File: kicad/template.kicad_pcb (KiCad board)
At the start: 2 copper layers, 84.1 x 61.7 mm, 7 parts, among them J1 Bus_PCI_Express_x1, J6 USB_C_Receptacle_USB2.0_16P, U1 MCP25625T-E/ML, U2 RP2040, U4 W25Q128JVP, X1 ABM8-272-T3, Y1 X322516MLB4SI

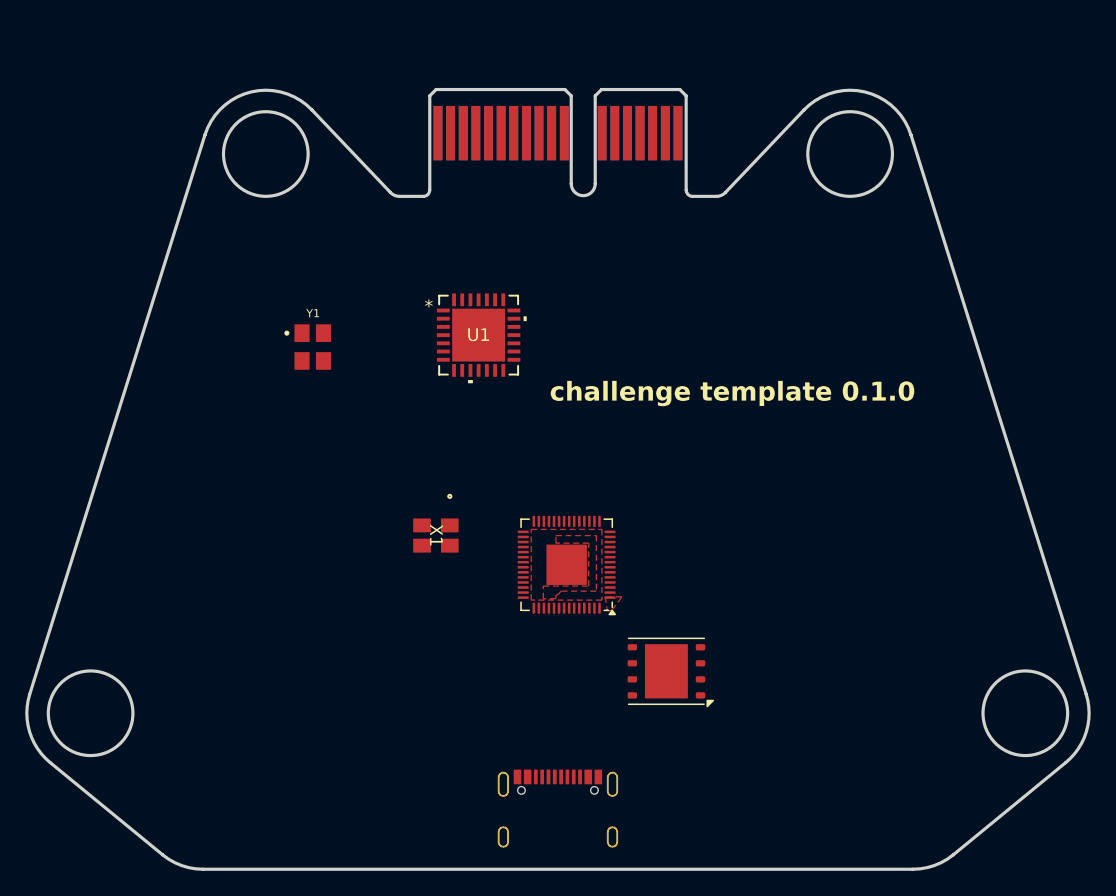
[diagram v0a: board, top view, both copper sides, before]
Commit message: Add LED array
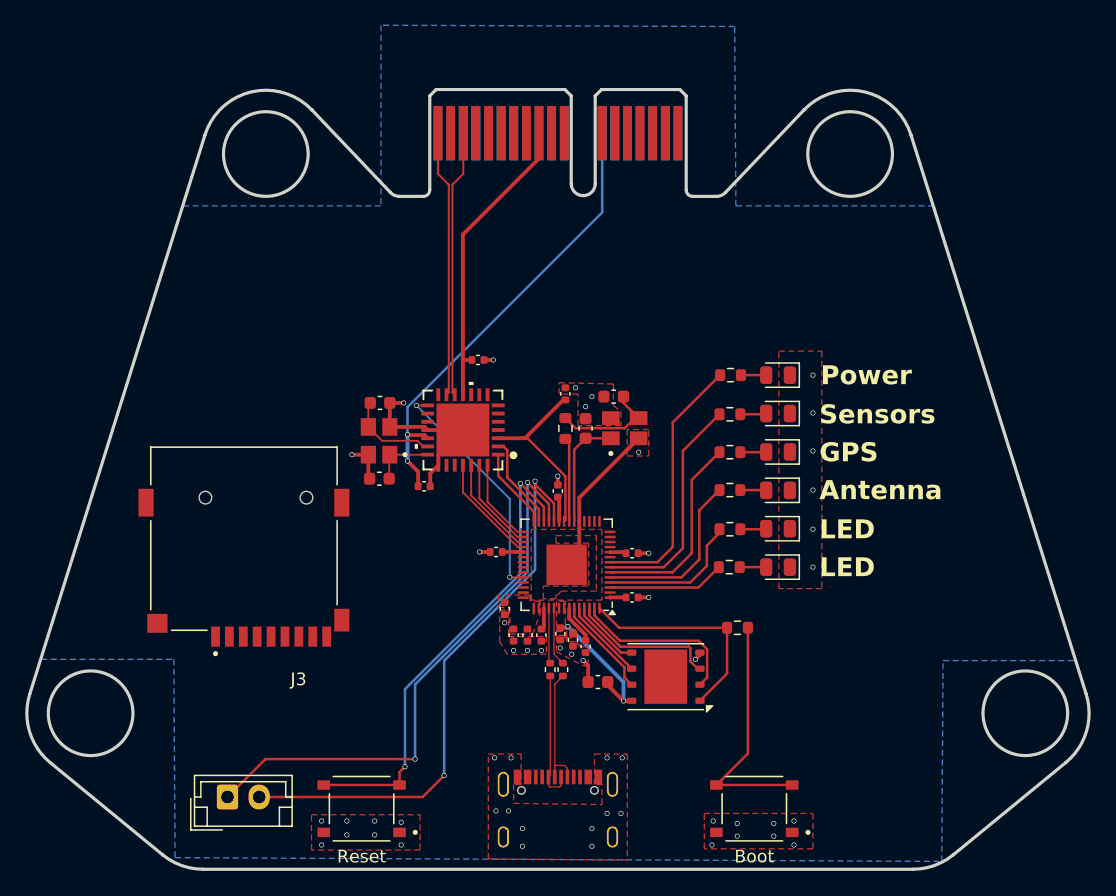
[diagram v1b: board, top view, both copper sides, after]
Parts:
- removed U1: MCP25625T-E/ML, challenge_template:QFN28_6X6MC_MCH
- added C1: 100n, Capacitor_SMD:C_0402_1005Metric, F.Cu at (142.9, 103.9)
- added C10: 100n, Capacitor_SMD:C_0402_1005Metric, F.Cu at (148.6, 104.8)
- added C11: 1uF, Capacitor_SMD:C_0402_1005Metric, F.Cu at (145.1, 103.9)
- added C12: 100n, Capacitor_SMD:C_0603_1608Metric, F.Cu at (149.6, 107.6)
- added C13: 15p, Capacitor_SMD:C_0603_1608Metric, F.Cu at (150.8, 85.0)
- added C14: 15p, Capacitor_SMD:C_0603_1608Metric, F.Cu at (148.6, 87.5)
- added C15: 100n, Capacitor_SMD:C_0402_1005Metric, F.Cu at (147.0, 84.8)
- added C16: 100n, Capacitor_SMD:C_0402_1005Metric, F.Cu at (140.1, 82.1)
- added C17: 100n, Capacitor_SMD:C_0402_1005Metric, F.Cu at (135.8, 92.1)
- added C18: 22p, Capacitor_SMD:C_0603_1608Metric, F.Cu at (132.3, 91.5)
- added C19: 22p, Capacitor_SMD:C_0603_1608Metric, F.Cu at (132.3, 85.5)
- added C2: 100n, Capacitor_SMD:C_0402_1005Metric, F.Cu at (152.3, 97.4)
- added C3: 100n, Capacitor_SMD:C_0402_1005Metric, F.Cu at (152.3, 100.9)
- added C4: 100n, Capacitor_SMD:C_0402_1005Metric, F.Cu at (141.5, 97.3)
- added C5: 100n, Capacitor_SMD:C_0402_1005Metric, F.Cu at (144.0, 103.9)
- added C6: 100n, Capacitor_SMD:C_0402_1005Metric, F.Cu at (147.6, 104.3)
- added C7: 100n, Capacitor_SMD:C_0402_1005Metric, F.Cu at (146.6, 103.8)
- added C8: 1uF, Capacitor_SMD:C_0402_1005Metric, F.Cu at (142.2, 101.8)
- added C9: 100n, Capacitor_SMD:C_0402_1005Metric, F.Cu at (146.4, 92.5)
- added D1: LED, LED_SMD:LED_0805_2012Metric, F.Cu at (163.8, 98.5)
- added D2: LED, LED_SMD:LED_0805_2012Metric, F.Cu at (163.8, 95.5)
- added D3: LED, LED_SMD:LED_0805_2012Metric, F.Cu at (163.8, 92.4)
- added D4: LED, LED_SMD:LED_0805_2012Metric, F.Cu at (163.8, 89.4)
- added D5: LED, LED_SMD:LED_0805_2012Metric, F.Cu at (163.8, 86.3)
- added D6: LED, LED_SMD:LED_0805_2012Metric, F.Cu at (163.8, 83.3)
- added J2: Conn_01x02, Connector_JST:JST_EH_B2B-EH-A_1x02_P2.50mm_Vertical, F.Cu at (120.2, 116.7)
- added J3: MSD-4-A, MSD_4_A:CUI_MSD-4-A, F.Cu at (121.5, 96.2)
- added R1: 27, Resistor_SMD:R_0402_1005Metric, F.Cu at (146.8, 106.6)
- added R10: 220, Resistor_SMD:R_0603_1608Metric, F.Cu at (160.1, 83.3)
- added R2: 27, Resistor_SMD:R_0402_1005Metric, F.Cu at (145.8, 106.6)
- added R3: 1k, Resistor_SMD:R_0603_1608Metric, F.Cu at (147.0, 87.5)
- added R4: 1k, Resistor_SMD:R_0603_1608Metric, F.Cu at (160.6, 103.3)
- added R5: 220, Resistor_SMD:R_0603_1608Metric, F.Cu at (160.0, 98.5)
- added R6: 220, Resistor_SMD:R_0603_1608Metric, F.Cu at (160.0, 95.5)
- added R7: 220, Resistor_SMD:R_0603_1608Metric, F.Cu at (160.0, 92.4)
- added R8: 220, Resistor_SMD:R_0603_1608Metric, F.Cu at (160.0, 89.4)
- added R9: 220, Resistor_SMD:R_0603_1608Metric, F.Cu at (160.0, 86.4)
- added S1: TS-1187A-B-A-B, TS-1187A-B-A-B:SW_TS-1187A-B-A-B, F.Cu at (162.0, 117.6)
- added S2: TS-1187A-B-A-B, TS-1187A-B-A-B:SW_TS-1187A-B-A-B, F.Cu at (130.9, 117.6)
- added U9: MCP25625T-E/ML, MCP25625T_E_ML:QFN28_6X6MC_MCH, F.Cu at (138.9, 87.6)
- X1: footprint challenge_template:ABM8-272-T3_ABR -> ABM8-272-T3:ABM8-272-T3_ABR
- Y1: footprint challenge_template:OSC_X322516MLB4SI -> X322516MLB4SI:OSC_X322516MLB4SI
- moved X1 17.2 mm to (151.7, 87.5), turned to 90 degrees
- moved Y1 9.09 mm to (132.2, 88.5), turned to 180 degrees
- moved U4 0.43 mm to (154.9, 107.2)
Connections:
- net Net-(J6-D+-PadA6) renamed USB_D+
- net Net-(J6-D--PadA7) renamed USB_D-
- U2 pad 1: Net-(U2-IOVDD-Pad1) -> +3.3V
- U2 pad 10: Net-(U2-IOVDD-Pad1) -> +3.3V
- U2 pad 12: unconnected-(U2-GPIO9-Pad12) -> CD
- U2 pad 19: unconnected-(U2-TESTEN-Pad19) -> GND
- U2 pad 20: unconnected-(U2-XIN-Pad20) -> /XIN
- U2 pad 21: unconnected-(U2-XOUT-Pad21) -> /XOUT
- U2 pad 22: Net-(U2-IOVDD-Pad1) -> +3.3V
- U2 pad 23: Net-(U2-DVDD-Pad23) -> +1.1V
- U2 pad 24: unconnected-(U2-SWCLK-Pad24) -> Net-(J2-Pin_2)
- U2 pad 25: unconnected-(U2-SWD-Pad25) -> Net-(J2-Pin_1)
- U2 pad 26: unconnected-(U2-RUN-Pad26) -> /RUN
- U2 pad 27: unconnected-(U2-GPIO16-Pad27) -> CANRESET
- U2 pad 28: unconnected-(U2-GPIO17-Pad28) -> CS
- U2 pad 29: unconnected-(U2-GPIO18-Pad29) -> SO
- U2 pad 3: unconnected-(U2-GPIO1-Pad3) -> Net-(U2-GPIO1)
- U2 pad 30: unconnected-(U2-GPIO19-Pad30) -> SI
- U2 pad 31: unconnected-(U2-GPIO20-Pad31) -> SCK
- U2 pad 32: unconnected-(U2-GPIO21-Pad32) -> CANINT
- U2 pad 33: Net-(U2-IOVDD-Pad1) -> +3.3V
- U2 pad 38: unconnected-(U2-GPIO26_ADC0-Pad38) -> CANSTBY
- U2 pad 4: unconnected-(U2-GPIO2-Pad4) -> Net-(U2-GPIO2)
- U2 pad 42: Net-(U2-IOVDD-Pad1) -> +3.3V
- U2 pad 43: unconnected-(U2-ADC_AVDD-Pad43) -> +3.3V
- U2 pad 44: unconnected-(U2-VREG_IN-Pad44) -> +3.3V
- U2 pad 45: unconnected-(U2-VREG_VOUT-Pad45) -> +1.1V
- U2 pad 46: unconnected-(U2-USB_DM-Pad46) -> Net-(U2-USB_DM)
- U2 pad 47: unconnected-(U2-USB_DP-Pad47) -> Net-(U2-USB_DP)
- U2 pad 48: unconnected-(U2-USB_VDD-Pad48) -> +3.3V
- U2 pad 49: Net-(U2-IOVDD-Pad1) -> +3.3V
- U2 pad 5: unconnected-(U2-GPIO3-Pad5) -> Net-(U2-GPIO3)
- U2 pad 50: Net-(U2-DVDD-Pad23) -> +1.1V
- U2 pad 51: unconnected-(U2-QSPI_SD3-Pad51) -> /QSPI_SD3
- U2 pad 52: unconnected-(U2-QSPI_SCLK-Pad52) -> /QSPI_SCLK
- U2 pad 53: unconnected-(U2-QSPI_SD0-Pad53) -> /QSPI_SD0
- U2 pad 54: unconnected-(U2-QSPI_SD2-Pad54) -> /QSPI_SD2
- U2 pad 55: unconnected-(U2-QSPI_SD1-Pad55) -> /QSPI_SD1
- U2 pad 56: unconnected-(U2-QSPI_SS-Pad56) -> /QSPI_SS
- U2 pad 57: unconnected-(U2-GND-Pad57) -> GND
- U2 pad 6: unconnected-(U2-GPIO4-Pad6) -> Net-(U2-GPIO4)
- U2 pad 7: unconnected-(U2-GPIO5-Pad7) -> Net-(U2-GPIO5)
- U2 pad 8: unconnected-(U2-GPIO6-Pad8) -> Net-(U2-GPIO6)
- U4 pad 1: unconnected-(U4-~{CS}-Pad1) -> /QSPI_SS
- U4 pad 2: unconnected-(U4-DO(IO1)-Pad2) -> /QSPI_SD1
- U4 pad 3: unconnected-(U4-IO2-Pad3) -> /QSPI_SD2
- U4 pad 4: unconnected-(U4-GND-Pad4) -> GND
- U4 pad 5: unconnected-(U4-DI(IO0)-Pad5) -> /QSPI_SD0
- U4 pad 6: unconnected-(U4-CLK-Pad6) -> /QSPI_SCLK
- U4 pad 7: unconnected-(U4-IO3-Pad7) -> /QSPI_SD3
- U4 pad 8: unconnected-(U4-VCC-Pad8) -> +3.3V
- X1 pad 1: unconnected-(X1-Pad1) -> /XIN
- X1 pad 2: unconnected-(X1-Pad2) -> GND
- X1 pad 3: unconnected-(X1-Pad3) -> Net-(C13-Pad1)
- X1 pad 4: unconnected-(X1-Pad4) -> GND
- Y1 pad 1: unconnected-(Y1-Pad1) -> OSC1
- Y1 pad 2: Net-(Y1-Pad2) -> GND
- Y1 pad 3: unconnected-(Y1-Pad3) -> OSC2
- Y1 pad 4: Net-(Y1-Pad2) -> GND
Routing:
- net +3.3V: track 0.00 -> 56.4 mm, vias 0 -> 2
- net Net-(J2-Pin_1): track 0.00 -> 45.5 mm, vias 0 -> 2
- net Net-(J2-Pin_2): track 0.00 -> 45.4 mm, vias 0 -> 2
- net +5V: track 0.00 -> 38.2 mm, vias 0 -> 2
- net GND: track 0.00 -> 38.1 mm, vias 0 -> 53
- net /RUN: track 0.00 -> 37.6 mm, vias 0 -> 2
- net CANP: track 0.00 -> 22.9 mm
- net CANN: track 0.00 -> 22.9 mm
- net Net-(U2-GPIO6): track 0.00 -> 20.6 mm
- net /~{USB_BOOT_S}: track 0.00 -> 19.5 mm
- net CANSTBY: track 0.00 -> 18.6 mm, vias 0 -> 2
- net Net-(U2-GPIO5): track 0.00 -> 18.2 mm
- net /QSPI_SS: track 0.00 -> 17.4 mm
- net Net-(U2-GPIO4): track 0.00 -> 16.0 mm
- net Net-(U2-GPIO3): track 0.00 -> 13.8 mm
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- added copper zone on F.Cu, net +1.1V
- added copper zone on B.Cu, net GND
- added copper zone on F.Cu, net GND
- removed copper zone on F.Cu, net unconnected-(U2-VREG_VOUT-Pad45)
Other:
- board text added: "Antenna"
- board text added: "Boot"
- board text added: "GPS"
- board text added: "LED"
- board text added: "Power"
- board text added: "Reset"
- board text added: "Sensors"
- board text removed: "challenge template 0.1.0"
